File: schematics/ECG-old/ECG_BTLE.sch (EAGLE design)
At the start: 53 parts, among them IC1 ADS1293, IC3 MCP1703, IC4 CC2541, X1-X XTAL-2SMD, X2 XTAL_403

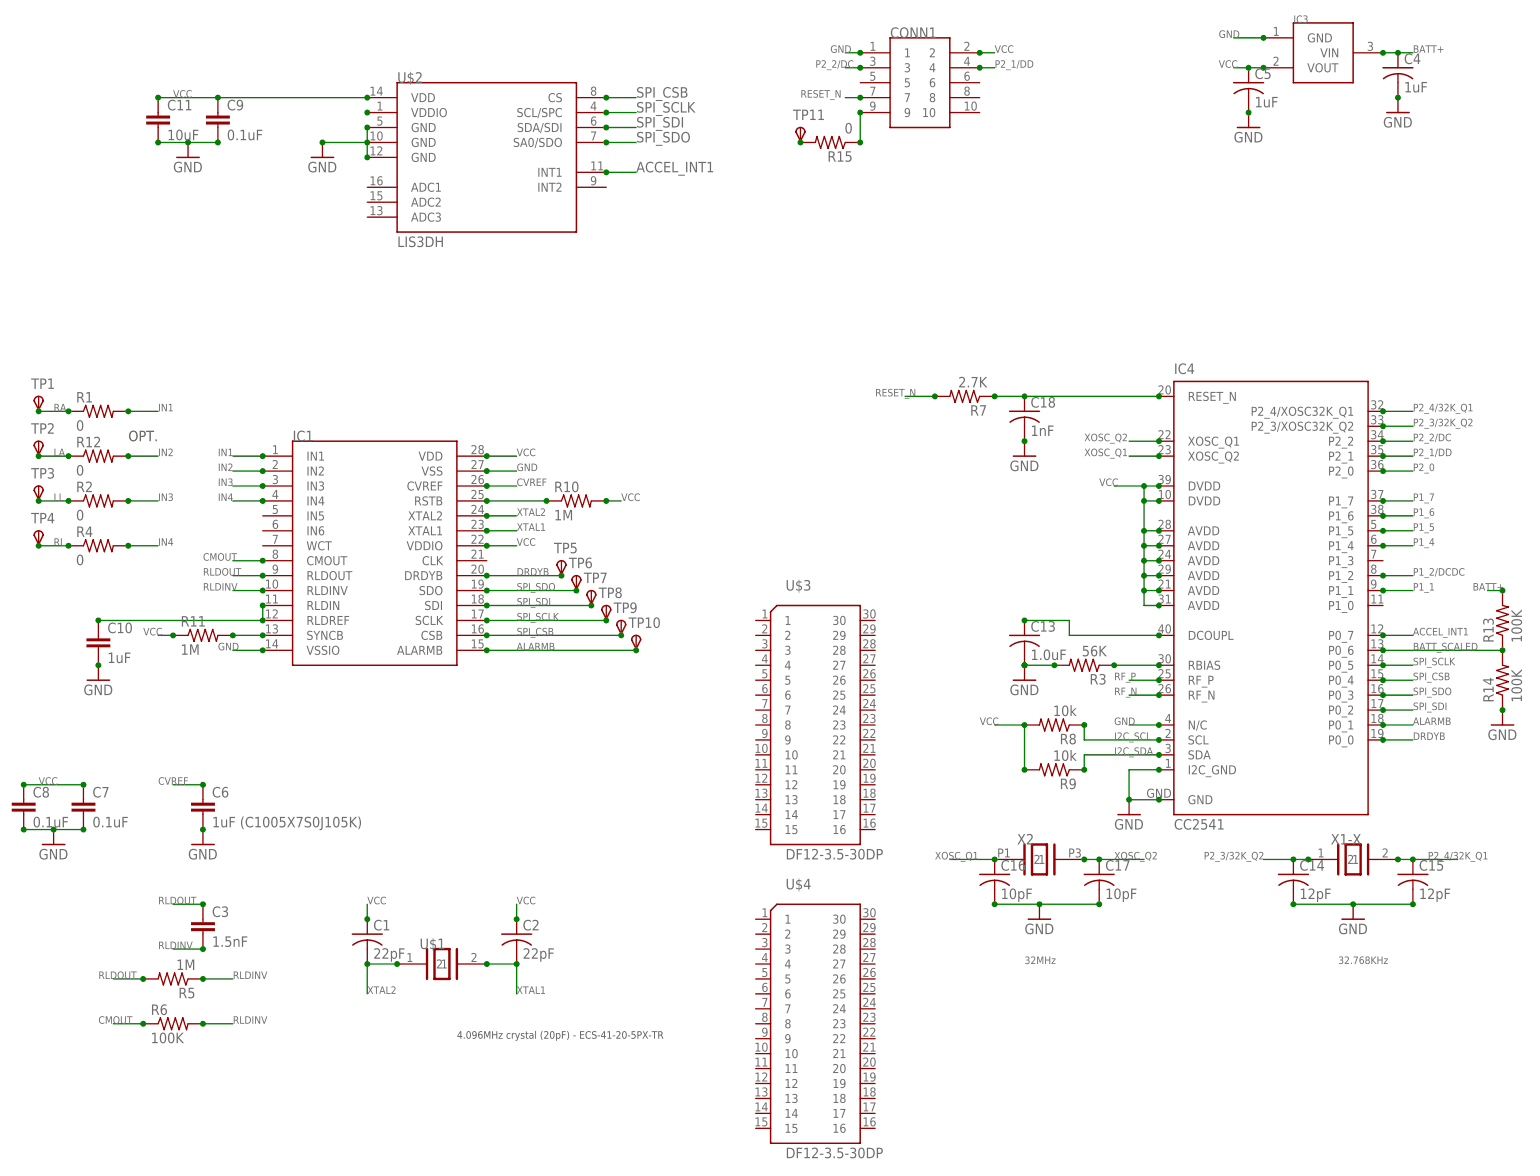
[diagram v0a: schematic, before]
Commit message: added analog switch for ads1293 power. added jumper for ads1293 xtal gnd/vcc connection
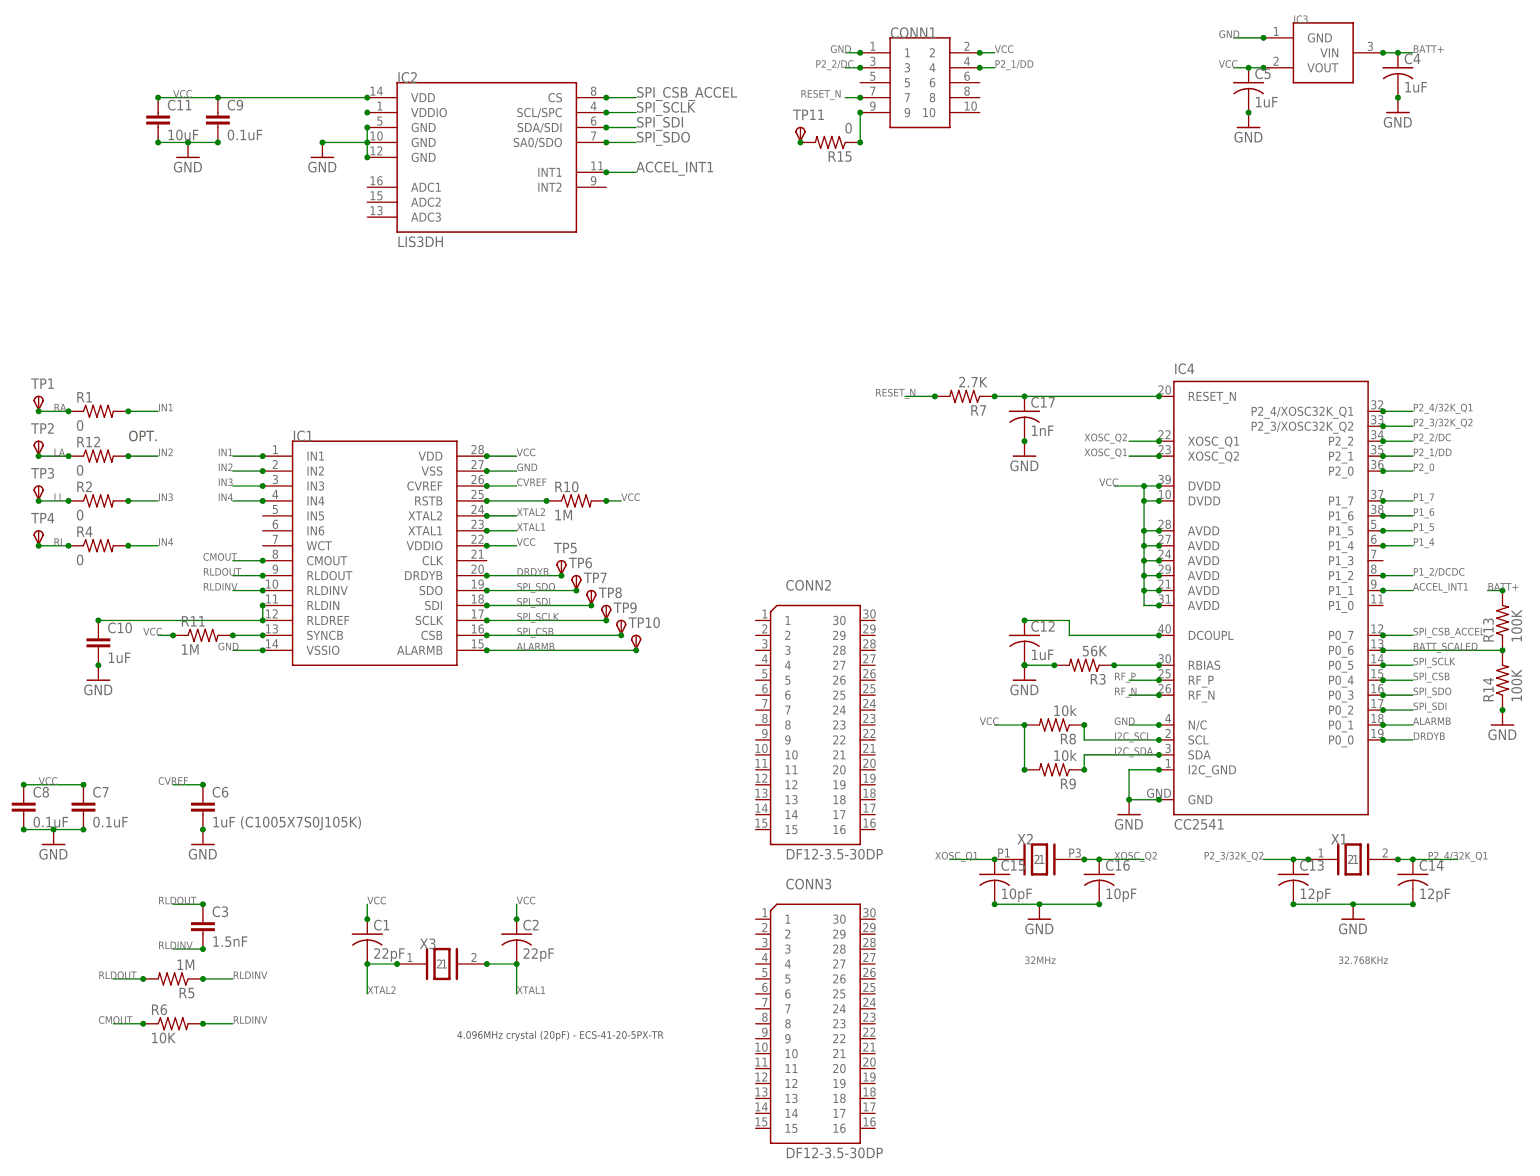
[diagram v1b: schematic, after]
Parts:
- removed C18: 1nF, rcl:C-USC0402
- added C12: 1uF, rcl:C-USC0402
- C13: value 1.0uF -> 12pF; device rcl:C-USC0402 -> rcl:C-USC0201
- C15: value 12pF -> 10pF
- C17: value 10pF -> 1nF; device rcl:C-USC0201 -> rcl:C-USC0402
- R6: value 100K -> 10K
- renumbered U$1 to X3, U$2 to IC2, U$3 to CONN2, U$4 to CONN3, X1-X to X1
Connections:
- removed net P1_1: IC4.P1_1
- new net SPI_CSB_ACCEL: IC2.CS, IC4.P0_7
- net ACCEL_INT1: now also IC4.P1_1; no longer IC4.P0_7
- net DCOUPL1: now also C12.1; no longer C13.1
- net GND: now also C12.2; no longer C18.2
- net N$8: now also C17.1; no longer C18.1
- net P2_3/32K_Q2: now also C13.1; no longer C14.1
- net P2_4/32K_Q1: now also C14.1; no longer C15.1
- net SPI_CSB: no longer IC2.CS
- net XOSC_Q1: now also C15.1; no longer C16.1
- net XOSC_Q2: now also C16.1; no longer C17.1
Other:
- moved on the sheet: C13, C14, C15, C16, C17
